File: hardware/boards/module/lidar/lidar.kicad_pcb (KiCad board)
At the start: 2 copper layers, 70.6 x 66 mm, 33 parts, among them J1 Conn_01x04_Socket, J2 Lidar, J3 Conn_01x03_Socket, J4 Conn_01x03_Socket, J5 Conn_01x03_Socket, J6 Conn_01x03_Socket, J7 Conn_01x05_Socket, J8 Conn_01x04_Socket, Q1 AO3401A, SW1 SW_Push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

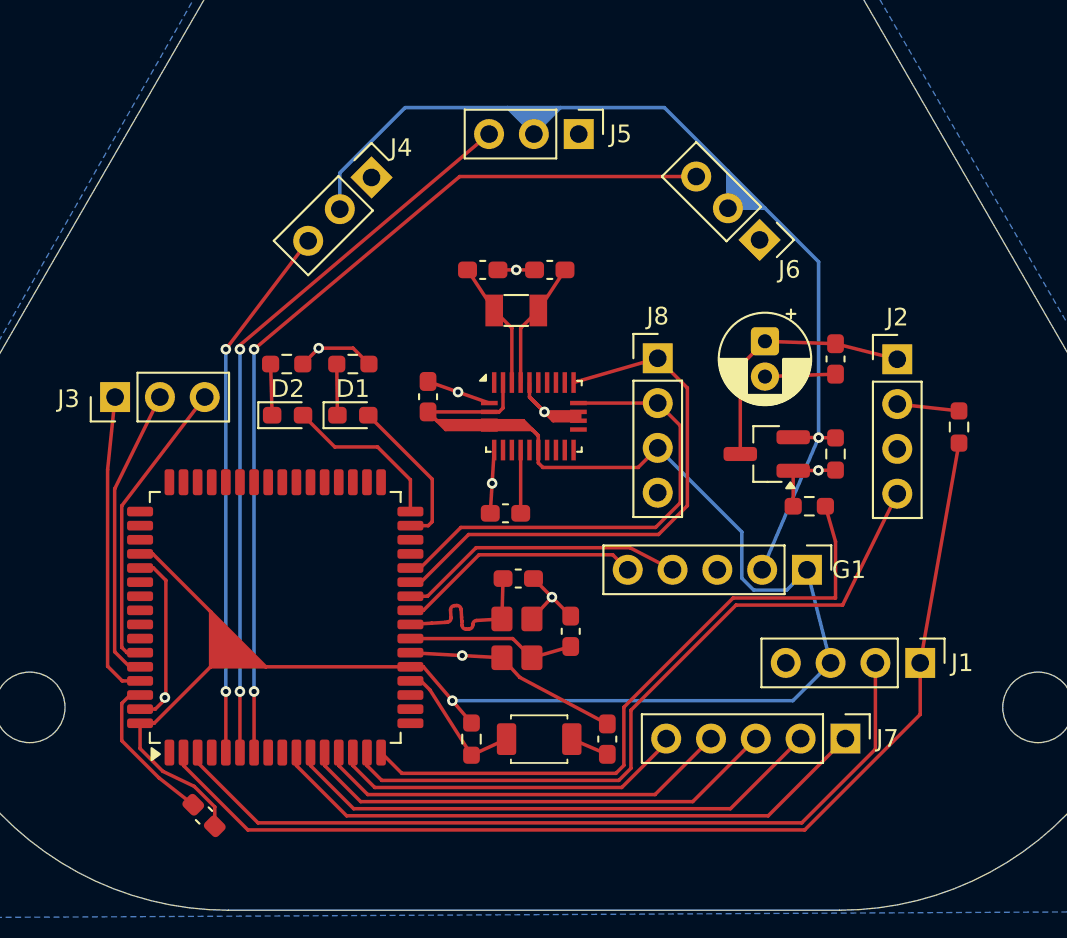
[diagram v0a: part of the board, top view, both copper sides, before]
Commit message: rounded tracks on lidar pcb
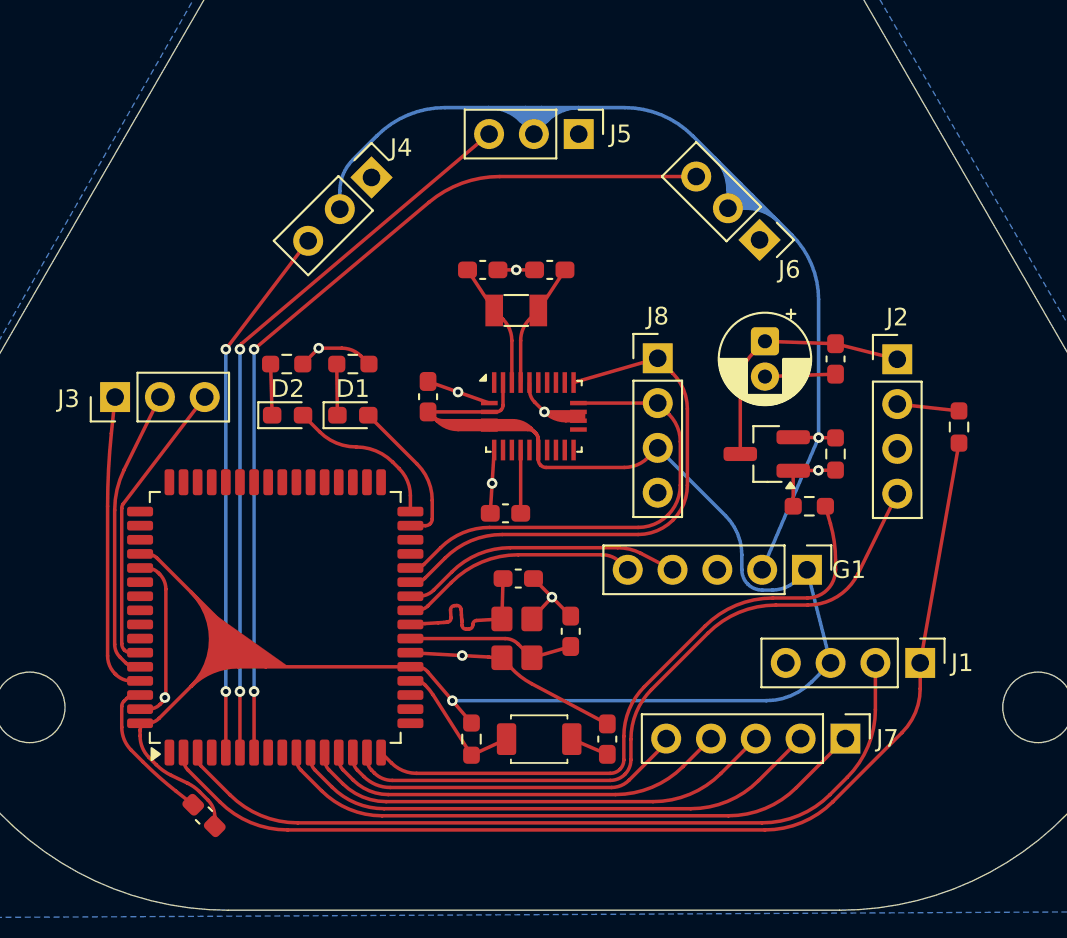
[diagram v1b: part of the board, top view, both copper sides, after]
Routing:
- net 5V: track 63.3 -> 69.5 mm
- net GND: track 56.7 -> 55.0 mm
- net LIDAR_EN: track 37.6 -> 36.2 mm
- net 3V3: track 112.3 -> 113.6 mm
- net LIDAR_PWM: track 41.1 -> 40.0 mm
- net TX0: track 47.0 -> 46.2 mm
- net RX0: track 62.3 -> 61.6 mm
- net RX1: track 31.5 -> 30.9 mm
- net TX1: track 27.5 -> 27.0 mm
- net DEBUG_0: track 34.9 -> 34.3 mm
- net DEBUG_1: track 31.2 -> 30.7 mm
